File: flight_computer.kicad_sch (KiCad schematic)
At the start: 11 parts, among them J1 Conn_01x13_Socket, J2 Conn_01x13_Socket, J3 Ignitor Output, J4 9v Battery Input, U1 CPC1002N, U2 CPC1002N, U3 CPC1002N, U4 BME280

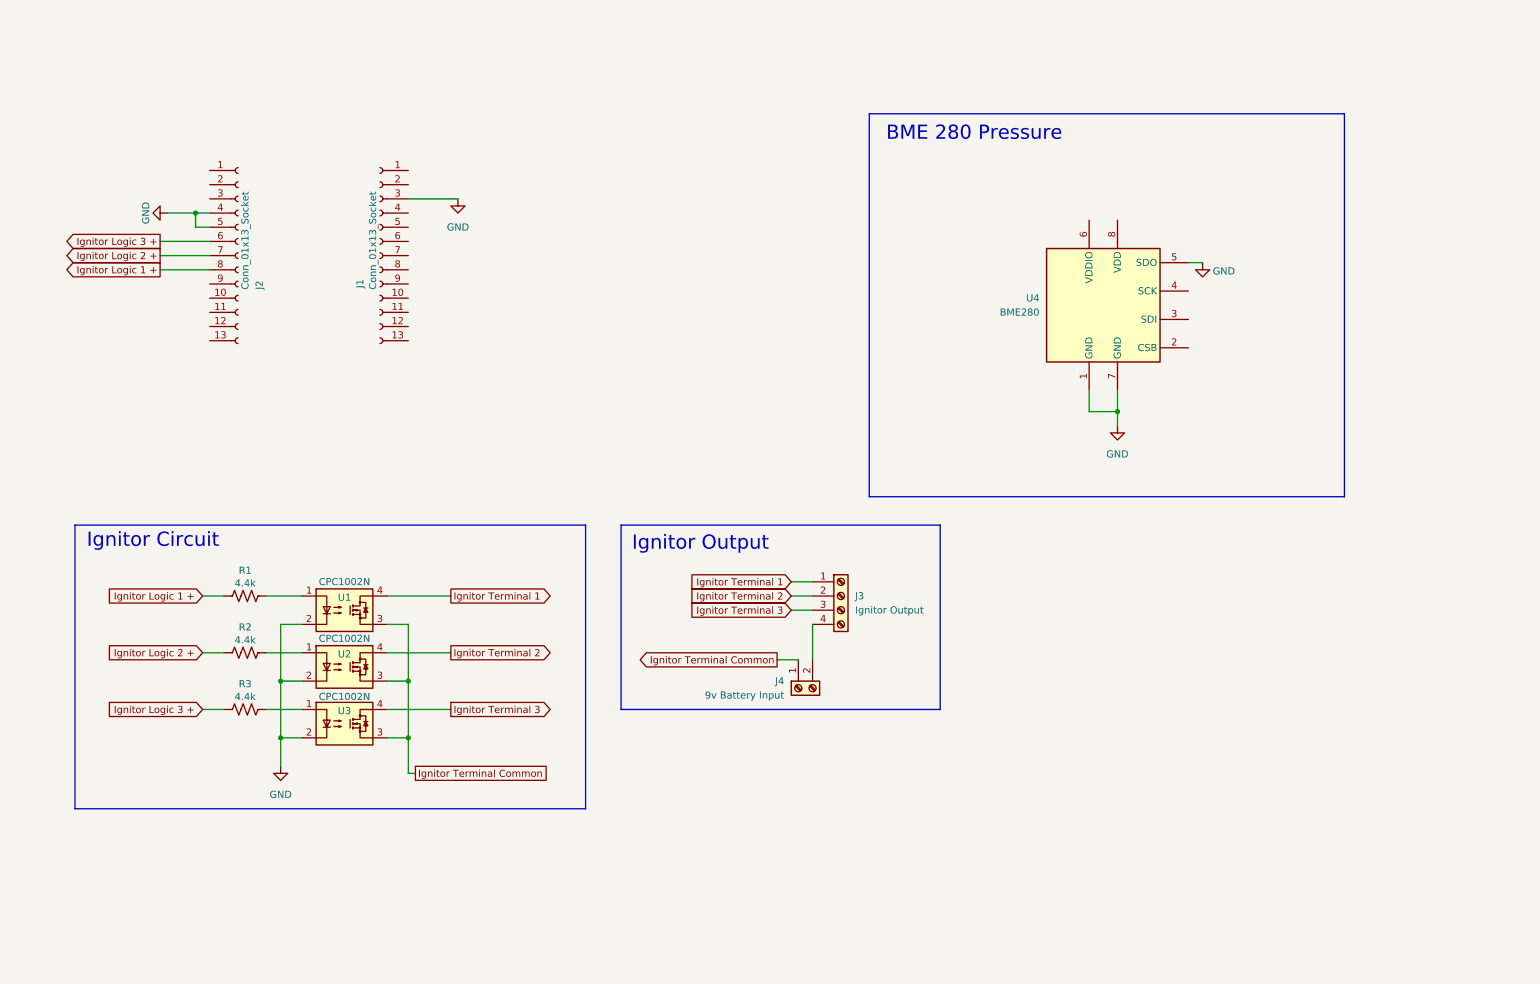
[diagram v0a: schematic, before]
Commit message: Layout finished for BNO055 and BME280
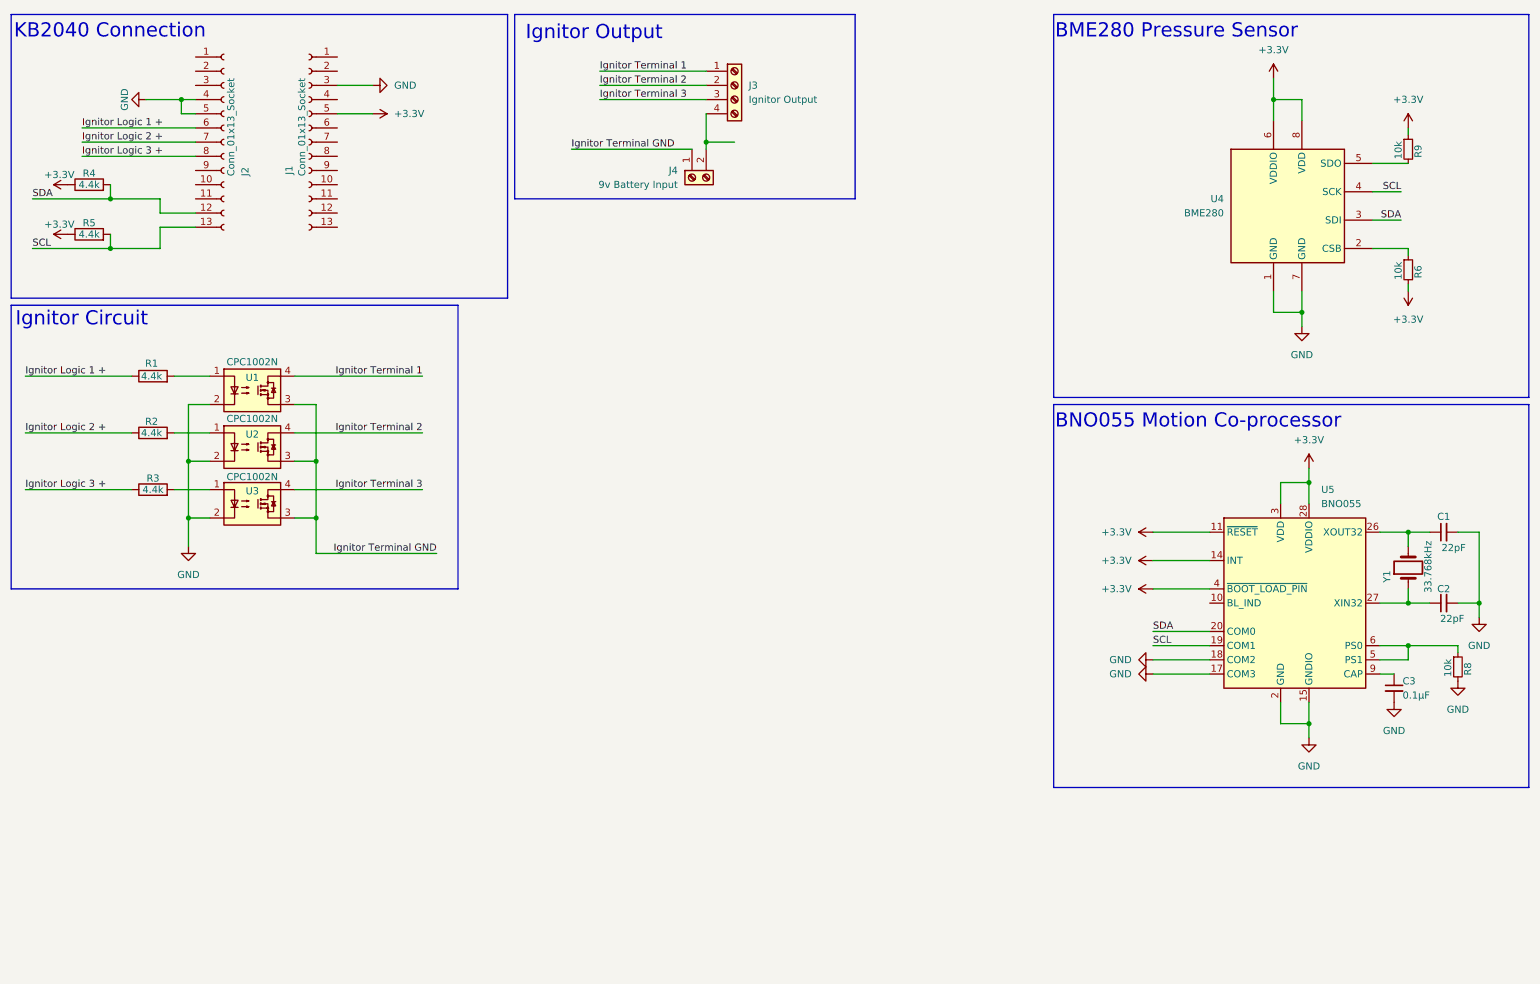
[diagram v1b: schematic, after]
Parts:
- removed R1, R2, R3: 4.4k, Resistor_SMD:R_0603_1608Metric_Pad0.98x0.95mm_HandSolder, symbol Device:R_US
- added C1, C2: 22pF, Capacitor_SMD:C_0603_1608Metric_Pad1.08x0.95mm_HandSolder, symbol Device:C_Small
- added C3: 0.1µF, Capacitor_SMD:C_0603_1608Metric_Pad1.08x0.95mm_HandSolder, symbol Device:C_Small
- added R1, R2, R3: 4.4k, Resistor_SMD:R_0603_1608Metric_Pad0.98x0.95mm_HandSolder, symbol Device:R
- added R4, R5: 4.4k, symbol Device:R
- added R6, R8, R9: 10k, Resistor_SMD:R_0603_1608Metric_Pad0.98x0.95mm_HandSolder, symbol Device:R_Small
- added U5: BNO055, Package_LGA:LGA-28_5.2x3.8mm_P0.5mm, symbol Sensor_Motion:BNO055
- added Y1: 33.768kHz, Crystal:Crystal_SMD_G8-2Pin_3.2x1.5mm_HandSoldering, symbol Device:Crystal
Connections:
- net GND: now also C1.2, C2.2, C3.2, R8.2, U5.15 (GNDIO), U5.16 (GNDIO), U5.17 (COM3), U5.18 (COM2), U5.2 (GND), U5.25 (GNDIO); no longer U4.5 (SDO)
- net Ignitor Logic 1 +: now also J2.6 (Pin_6), R1.1; no longer J2.8 (Pin_8)
- net Ignitor Logic 2 +: now also R2.1
- net Ignitor Logic 3 +: now also J2.8 (Pin_8), R3.1; no longer J2.6 (Pin_6)
- net at U3.1: now also R3.2
- net at U1.1: now also R1.2
- net +3.3V: now reaches J1.5 (Pin_5)
- net +3.3V: now also U4.6 (VDDIO), U4.8 (VDD), R4.1, R5.1, R6.2, R9.1, U5.11 (~{RESET}), U5.14 (INT), U5.28 (VDDIO), U5.3 (VDD), U5.4 (~{BOOT_LOAD_PIN})
- net SDA: now reaches J2.12 (Pin_12)
- net SDA: now also U4.3 (SDI), R4.2, U5.20 (COM0)
- net SCL: now reaches J2.13 (Pin_13)
- net SCL: now also U4.4 (SCK), R5.2, U5.19 (COM1)
- net at U2.1: now also R2.2
- net at U4.2 (CSB): now also R6.1
- net Ignitor Terminal Common renamed Ignitor Terminal GND
- new net: R9.2, U4.5 (SDO)
- new net: C3.1, U5.9 (CAP)
- new net: C2.1, U5.27 (XIN32), Y1.1
- new net: C1.1, U5.26 (XOUT32), Y1.2
- new net: R8.1, U5.5 (PS1), U5.6 (PS0)
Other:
- note added: "BME280 Pressure Sensor"
- note added: "BNO055 Motion Co-processor"
- note added: "KB2040 Connection"
- note removed: "BME 280 Pressure"
- moved on the sheet: J1, J2, J3, J4, U1, U2, U3, U4

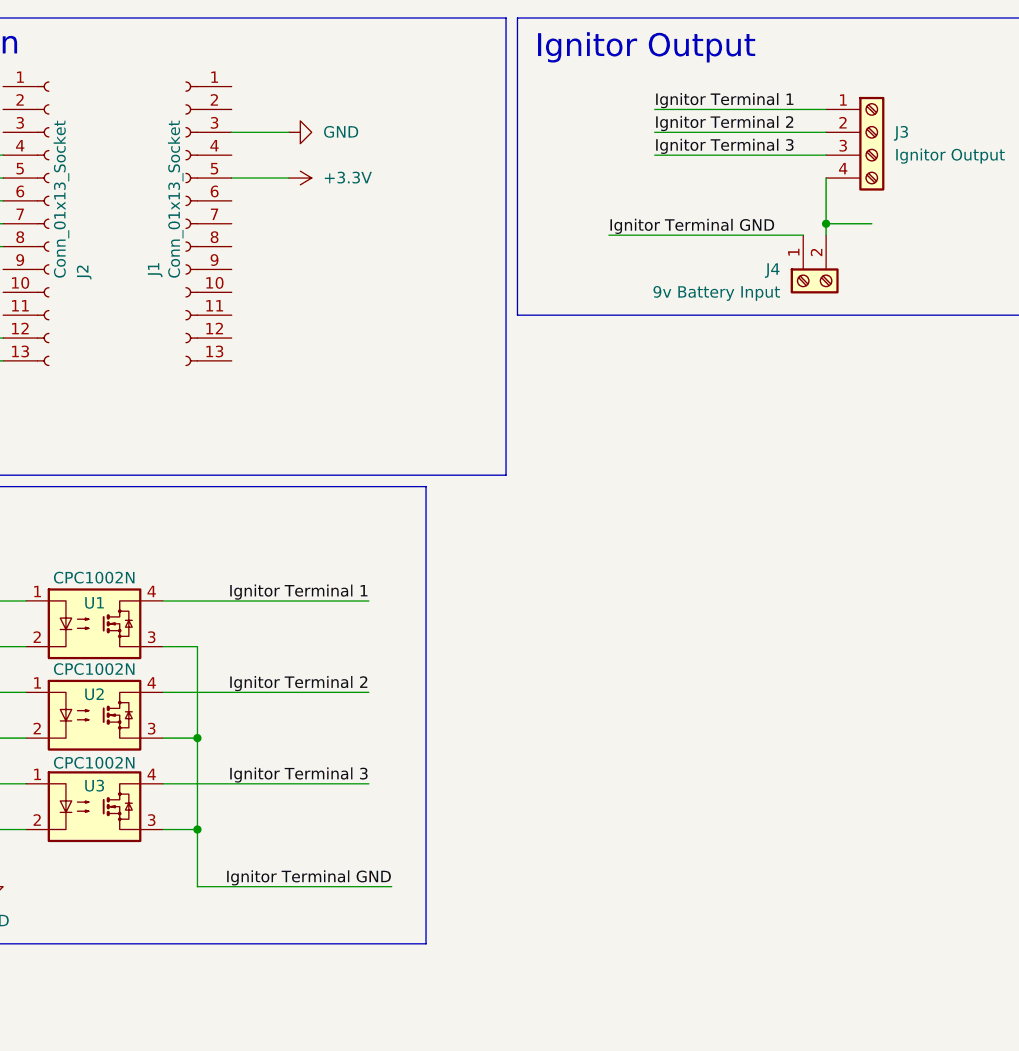
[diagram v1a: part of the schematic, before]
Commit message: Completed sensor layout
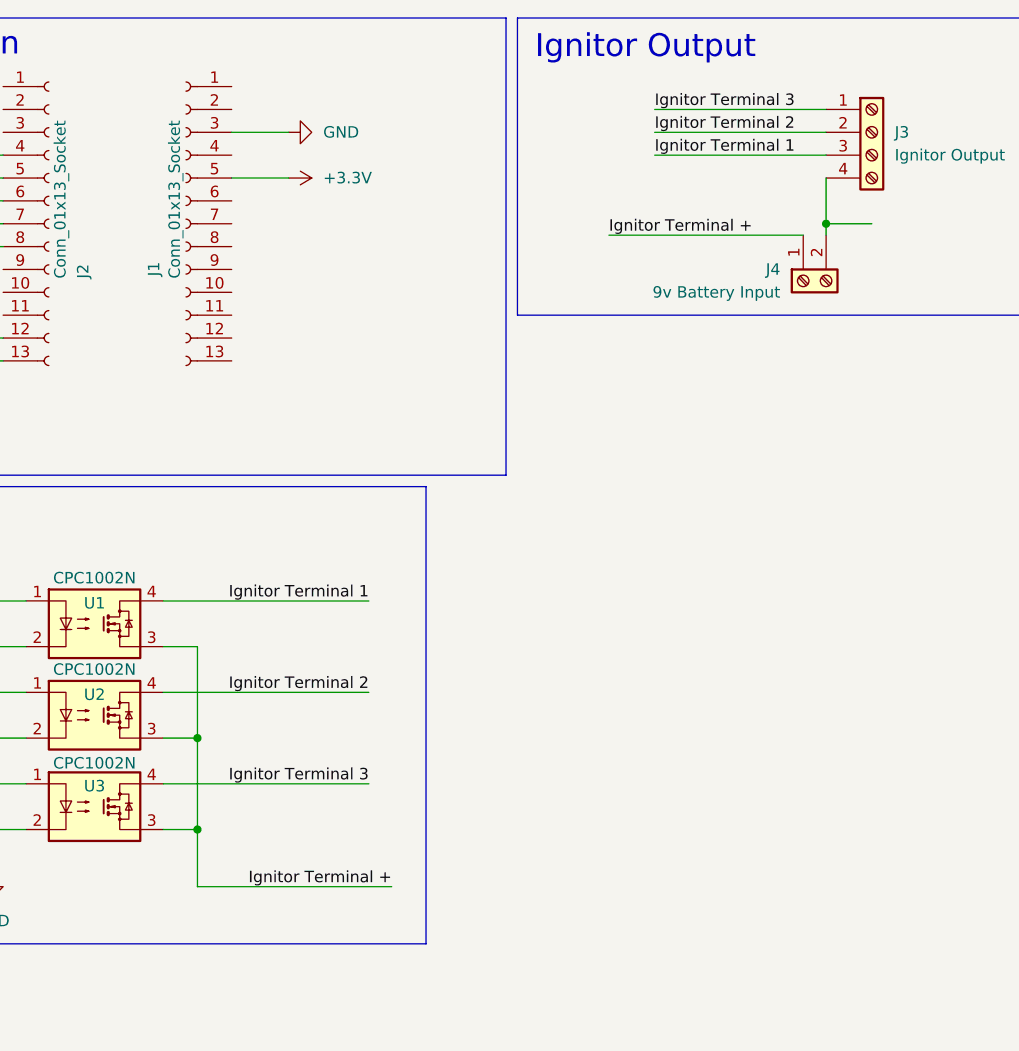
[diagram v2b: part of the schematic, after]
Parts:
- R4, R5: footprint (none) -> Resistor_SMD:R_0603_1608Metric_Pad0.98x0.95mm_HandSolder
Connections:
- net Ignitor Terminal 1: now also J3.3 (Pin_3); no longer J3.1 (Pin_1)
- net Ignitor Terminal 3: now also J3.1 (Pin_1); no longer J3.3 (Pin_3)
- net Ignitor Terminal GND renamed Ignitor Terminal +
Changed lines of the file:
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@@
+		)
+	)
+	(label "Ignitor Terminal 2"
+		(at 118.11 25.4 0)
+		(fields_autoplaced yes)
+		(effects
+			(font
+				(size 1.27 1.27)
+			)
+			(justify left bottom)
 		)
 	)
@@
 		)
 	)
-	(label "Ignitor Terminal 2"
-		(at 118.11 25.4 0)
-		(fields_autoplaced yes)
-		(effects
-			(font
-				(size 1.27 1.27)
-			)
-			(justify left bottom)
-		)
-	)
 	(label "SCL"
 		(at 16.51 54.61 0)
@@
 		)
 	)
+	(label "Ignitor Terminal 3"
+		(at 118.11 22.86 0)
+		(fields_autoplaced yes)
+		(effects
+			(font
+				(size 1.27 1.27)
+			)
+			(justify left bottom)
+		)
+	)
 	(label "Ignitor Logic 1 +"
 		(at 25.4 33.02 0)
@@
 		)
 	)
-	(label "Ignitor Terminal GND"
+	(label "Ignitor Terminal 1"
+		(at 118.11 27.94 0)
+		(fields_autoplaced yes)
+		(effects
+			(font
+				(size 1.27 1.27)
+			)
+			(justify left bottom)
+		)
+	)
+	(label "Ignitor Terminal +"
 		(at 88.9 109.22 180)
 		(fields_autoplaced yes)
@@
 		)
 	)
-	(label "Ignitor Terminal GND"
+	(label "Ignitor Terminal +"
 		(at 113.03 36.83 0)
 		(fields_autoplaced yes)
@@
 		)
 	)
-	(label "Ignitor Terminal 3"
-		(at 118.11 27.94 0)
-		(fields_autoplaced yes)
-		(effects
-			(font
-				(size 1.27 1.27)
-			)
-			(justify left bottom)
-		)
-	)
 	(label "SDA"
 		(at 261.62 49.53 180)
@@
 	(label "Ignitor Logic 2 +"
 		(at 15.24 87.63 0)
-		(fields_autoplaced yes)
-		(effects
-			(font
-				(size 1.27 1.27)
-			)
-			(justify left bottom)
-		)
-	)
-	(label "Ignitor Terminal 1"
-		(at 118.11 22.86 0)
 		(fields_autoplaced yes)
 		(effects
@@
 			)
 		)
-		(property "Footprint" ""
+		(property "Footprint" "Resistor_SMD:R_0603_1608Metric_Pad0.98x0.95mm_HandSolder"
 			(at 26.67 53.848 90)
 			(effects
@@
 			)
 		)
-		(property "Footprint" ""
+		(property "Footprint" "Resistor_SMD:R_0603_1608Metric_Pad0.98x0.95mm_HandSolder"
 			(at 26.67 44.958 90)
 			(effects

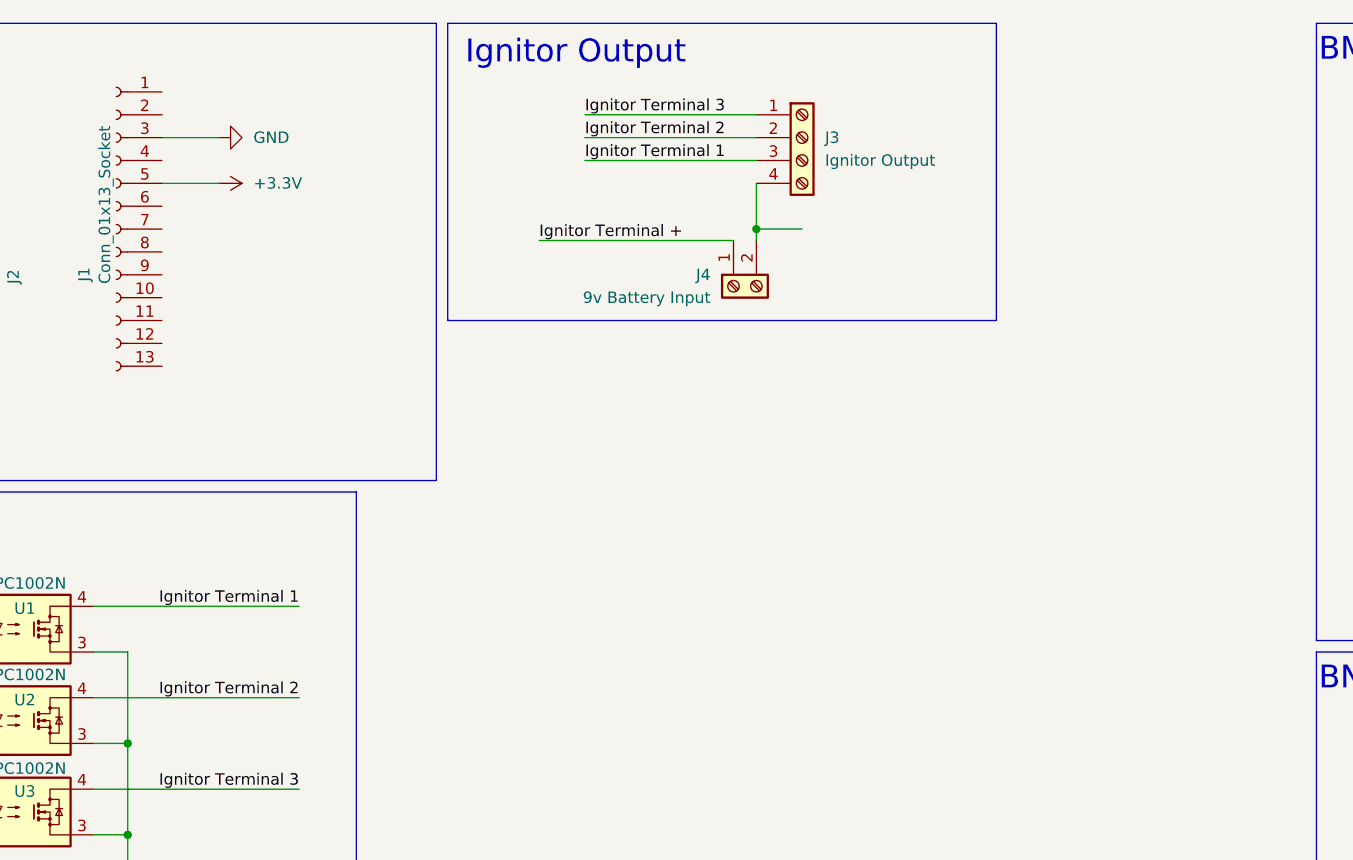
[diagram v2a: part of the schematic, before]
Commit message: Added voltage regulator
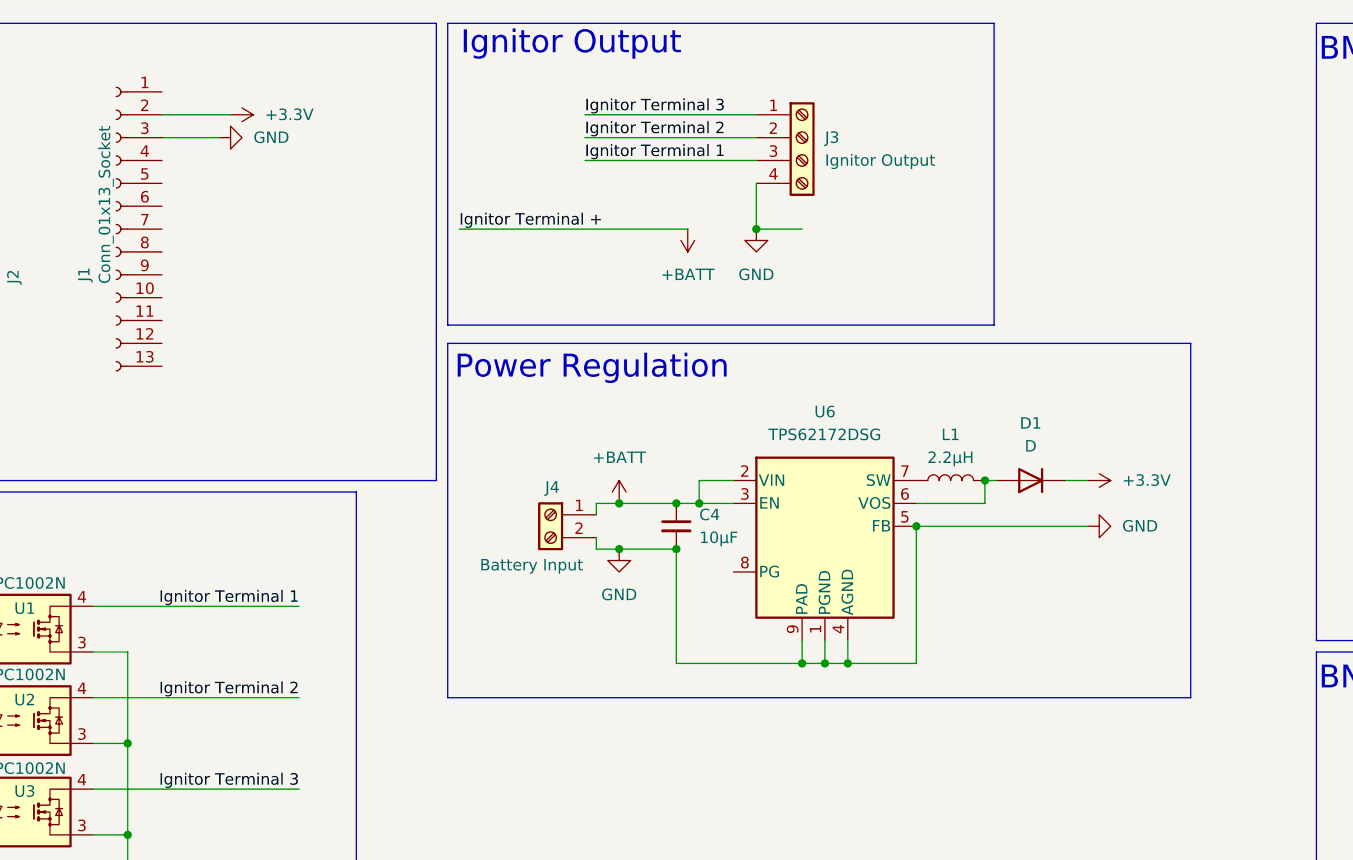
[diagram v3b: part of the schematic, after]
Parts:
- added C4: 10µF, Capacitor_SMD:C_0603_1608Metric_Pad1.08x0.95mm_HandSolder, symbol Device:C_Small
- added D1: D, Diode_SMD:D_0603_1608Metric_Pad1.05x0.95mm_HandSolder, symbol Device:D
- added L1: 2.2µH, Inductor_SMD:L_0603_1608Metric_Pad1.05x0.95mm_HandSolder, symbol Device:L
- added U6: TPS62172DSG, Package_SON:WSON-8-1EP_2x2mm_P0.5mm_EP0.9x1.6mm_ThermalVias, symbol Regulator_Switching:TPS62172DSG
- J4: value 9v Battery Input -> Battery Input
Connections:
- net +3.3V: now also J1.2 (Pin_2), D1.1 (K); no longer J1.5 (Pin_5)
- net GND: now also J3.4 (Pin_4), J4.2 (Pin_2), C4.2, U6.1 (PGND), U6.4 (AGND), U6.5 (FB), U6.9 (PAD)
- net Ignitor Terminal + renamed +BATT
- net +BATT: now also C4.1, U6.2 (VIN), U6.3 (EN)
- new net: D1.2 (A), L1.2, U6.6 (VOS)
- new net: L1.1, U6.7 (SW)
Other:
- note added: "Power Regulation"
- moved on the sheet: J4
